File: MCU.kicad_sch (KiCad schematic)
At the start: 16 parts, among them J2 ST-LINK_Header, U3 STM32F405RGT6, Y1 12MHz

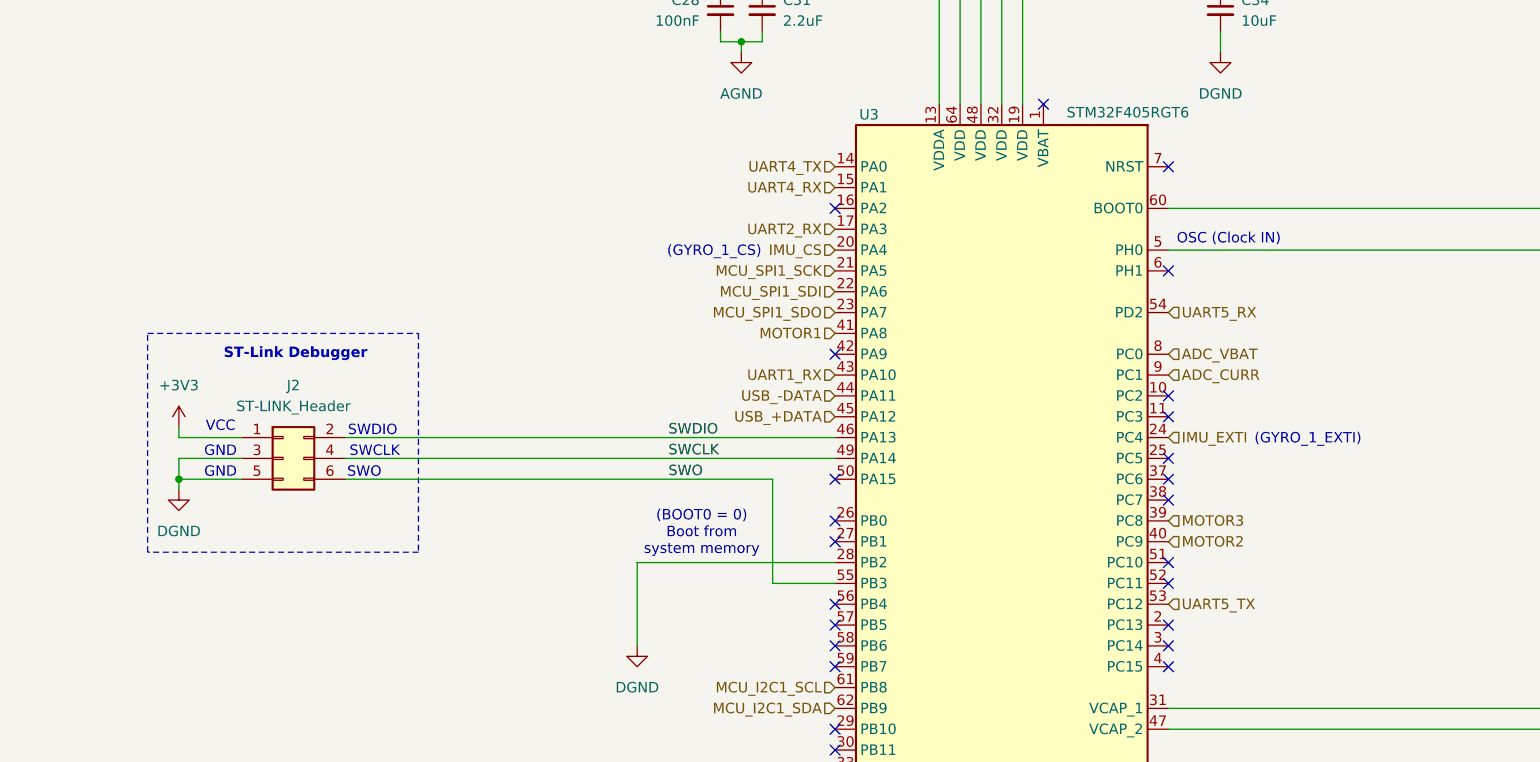
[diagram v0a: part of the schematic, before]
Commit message: Added debugger pads, needs to fix LED
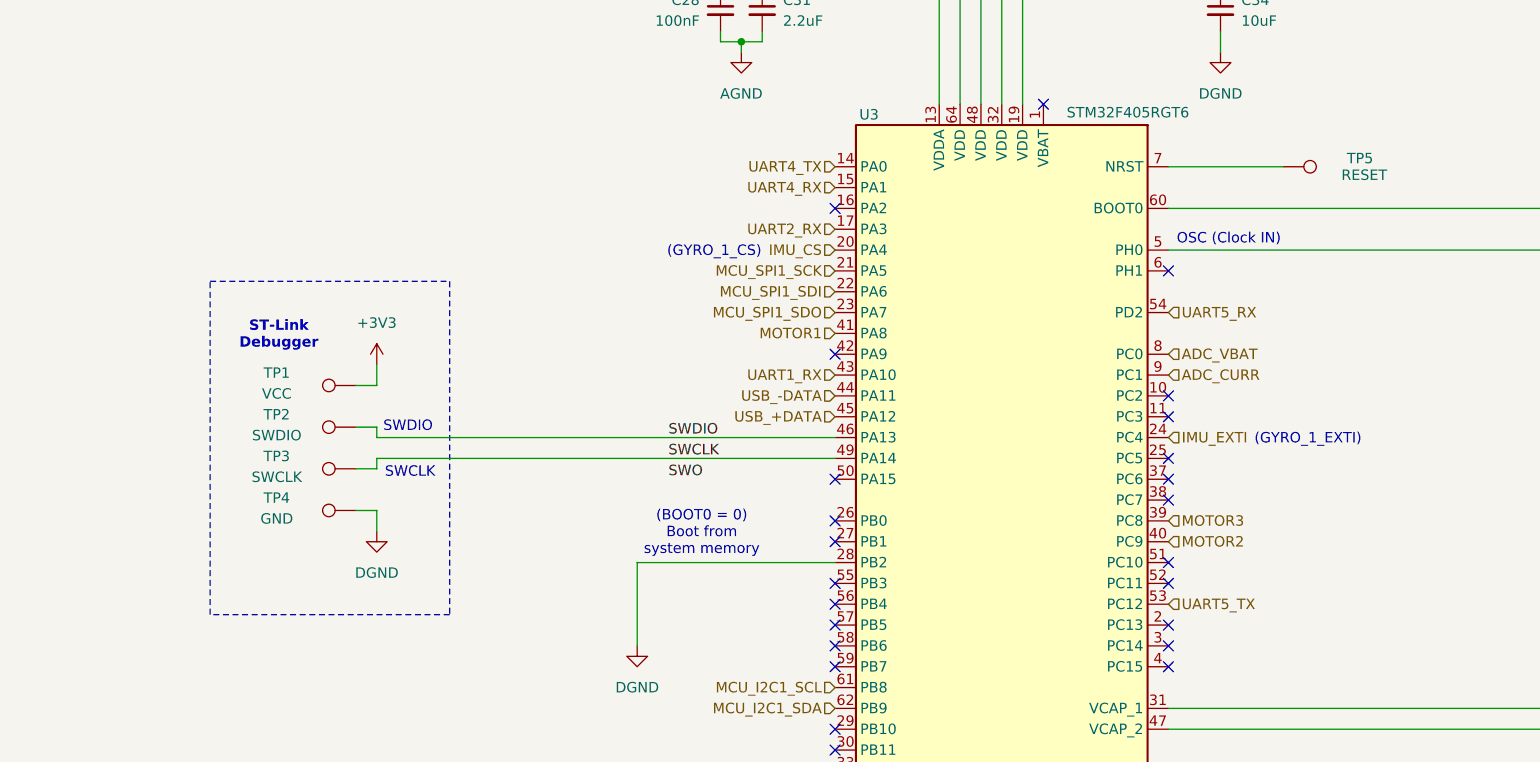
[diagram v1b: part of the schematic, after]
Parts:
- removed J2: ST-LINK_Header, Connector_PinHeader_1.27mm:PinHeader_2x03_P1.27mm_Vertical_SMD, symbol KSE_connectors:ST-LINK_Header
- added TP1: VCC, TestPoint:TestPoint_Pad_2.0x2.0mm, symbol Connector:TestPoint
- added TP2: SWDIO, TestPoint:TestPoint_Pad_2.0x2.0mm, symbol Connector:TestPoint
- added TP3: SWCLK, TestPoint:TestPoint_Pad_2.0x2.0mm, symbol Connector:TestPoint
- added TP4: GND, TestPoint:TestPoint_Pad_2.0x2.0mm, symbol Connector:TestPoint
- added TP5: RESET, TestPoint:TestPoint_Pad_2.0x2.0mm, symbol Connector:TestPoint
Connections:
- net +3V3: now also TP1.1
- net DGND: now also TP4.1
- net SWCLK: now also TP3.1
- net SWDIO: now also TP2.1
- net SWO: no longer U3.55 (PB3)
- net at U3.7 (NRST): now also TP5.1
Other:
- note removed: "GND"
- note removed: "SWO"
- note removed: "VCC"

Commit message: Finished DRC/ERC
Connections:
- net LED1: now reaches U3.26 (PB0)
- net LED0: now reaches U3.27 (PB1)
- no-connect marks 27 -> 25
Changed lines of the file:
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@@
-	)
-	(no_connect
-		(at 130.81 97.79)
 	)
 	(no_connect
@@
 	(no_connect
 		(at 171.45 107.95)
-	)
-	(no_connect
-		(at 130.81 95.25)
 	)
 	(no_connect
@@
 		)
 	)
-	(label "SWO"
-		(at 110.49 90.17 0)
-		(effects
-			(font
-				(size 1.27 1.27)
-			)
-			(justify left bottom)
-		)
-	)
 	(label "DFU_Enable"
 		(at 232.41 48.26 0)
@@
 		)
 	)
+	(hierarchical_label "LED0"
+		(shape input)
+		(at 130.81 97.79 180)
+		(effects
+			(font
+				(size 1.27 1.27)
+			)
+			(justify right)
+		)
+	)
 	(hierarchical_label "ADC_CURR"
 		(shape input)
@@
 		(effects
 			(font
+				(size 1.27 1.27)
+			)
+			(justify right)
+		)
+	)
+	(hierarchical_label "LED1"
+		(shape input)
+		(at 130.81 95.25 180)
+		(effects
+			(font
